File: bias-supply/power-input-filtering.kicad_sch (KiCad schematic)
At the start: 13 parts

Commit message: Updates for new bubba board
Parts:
- removed FL1, FL2: Choke_Coilcraft_MSD1278, MSD1278:MSD1278, symbol MSD1278:MSD1278
- added +V1: +V, bias-supply:TestPoint_THTPad_D2.0mm_Drill1.0mm_JLCrules, symbol Connector:TestPoint
- added -V1: -V, bias-supply:TestPoint_THTPad_D2.0mm_Drill1.0mm_JLCrules, symbol Connector:TestPoint
- added COM1: COM, bias-supply:TestPoint_THTPad_D2.0mm_Drill1.0mm_JLCrules, symbol Connector:TestPoint
- added FL1, FL2: Choke_Coilcraft_MSD1278, bias-supply:MSD1278, symbol bias-supply:MSD1278
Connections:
- net +V: now also +V1.1, FL1.4
- net -V: now also -V1.1, FL2.3
- net GND: no longer L1.2
- net COM IN: now reaches JP1.2 (B)
- net COM IN: now also C1.2, C2.2, C3.2, C4.2, JP2.1 (A), L1.1
- net +Vin renamed +VIN
- net +VIN: now also FL1.2
- net -Vin renamed -VIN
- net -VIN: now also FL2.1
- removed net REF: C1.2, C2.2, C3.2, C4.2, JP1.1 (A), JP2.2 (B), L1.1
- new net: FL1.1, JP1.1 (A)
- new net: FL2.2, JP2.2 (B)
- new net COM OUT: COM1.1, FL1.3, FL2.4, L1.2
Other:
- title: (none) -> Power input filtering
- moved on the sheet: C1, C2, C3, C4, C5, C6, C7, C8, L1

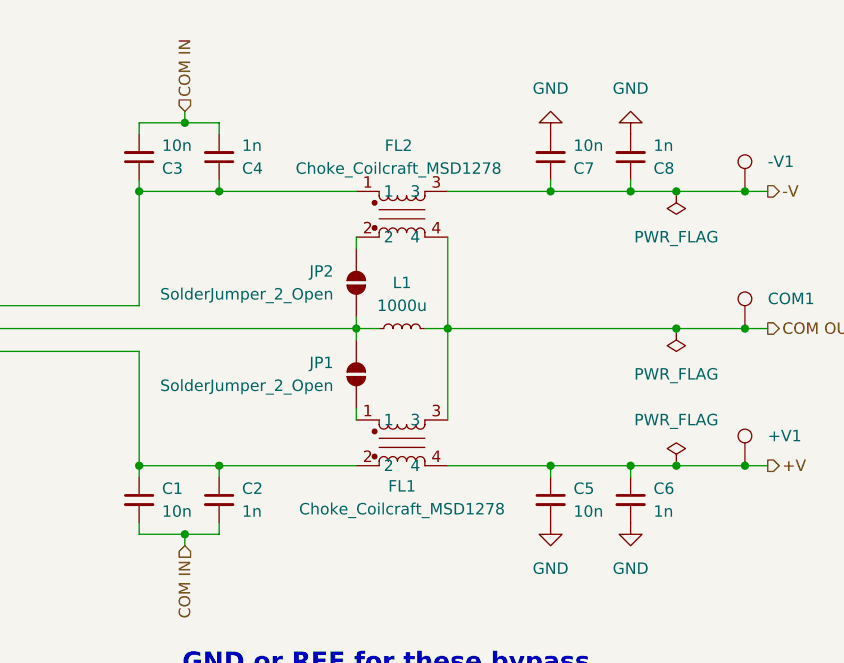
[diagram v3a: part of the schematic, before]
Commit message: Add fuses; change to coax; fixed I2C gnd
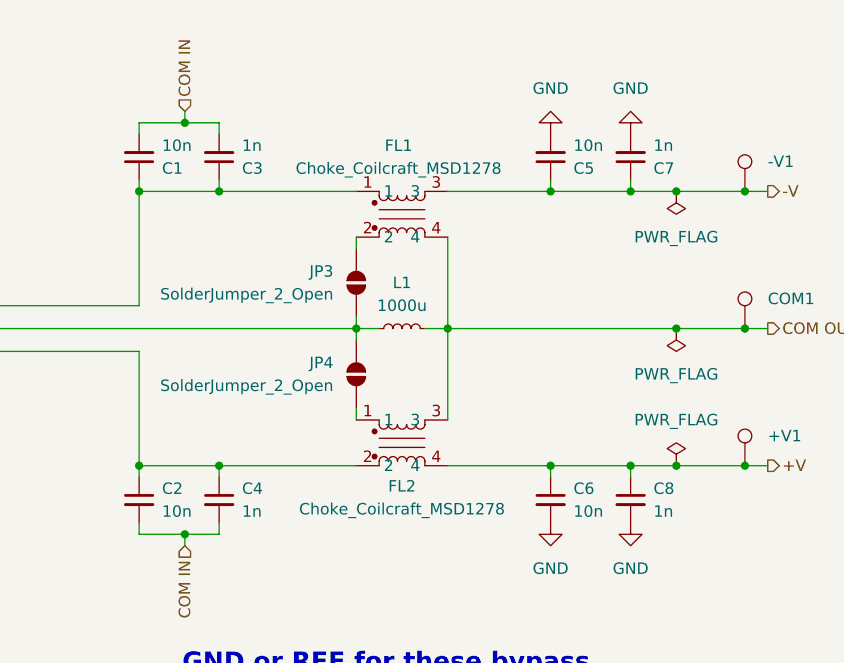
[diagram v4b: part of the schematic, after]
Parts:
- renumbered C3 to C1, C1 to C2, C4 to C3, C2 to C4, C7 to C5, C5 to C6, C8 to C7, C6 to C8, FL2 to FL1, FL1 to FL2, JP2 to JP3, JP1 to JP4
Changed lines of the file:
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@@
 		(dnp no)
 		(fields_autoplaced yes)
-		(property "Reference" "#PWR036"
+		(property "Reference" "#PWR05"
 			(at 166.37 114.3 0)
 			(effects
@@
 			(project "bias-supply"
 				(path "/f3205b63-fc57-4ea3-95d4-2a447f249c30/00549f8c-b970-4cd6-9099-4f1937ad6dc3"
-					(reference "#PWR036")
+					(reference "#PWR05")
 					(unit 1)
 				)
@@
 		(dnp no)
 		(fields_autoplaced yes)
-		(property "Reference" "#PWR034"
+		(property "Reference" "#PWR04"
 			(at 166.37 58.42 0)
 			(effects
@@
 			(project "bias-supply"
 				(path "/f3205b63-fc57-4ea3-95d4-2a447f249c30/00549f8c-b970-4cd6-9099-4f1937ad6dc3"
-					(reference "#PWR034")
+					(reference "#PWR04")
 					(unit 1)
 				)
@@
 		(on_board yes)
 		(dnp no)
-		(property "Reference" "FL1"
+		(property "Reference" "FL2"
 			(at 149.86 103.886 0)
 			(effects
@@
 			(project ""
 				(path "/f3205b63-fc57-4ea3-95d4-2a447f249c30/00549f8c-b970-4cd6-9099-4f1937ad6dc3"
-					(reference "FL1")
+					(reference "FL2")
 					(unit 1)
 				)
@@
 		(on_board yes)
 		(dnp no)
-		(property "Reference" "C8"
+		(property "Reference" "C7"
 			(at 177.8 68.5737 0)
 			(effects
@@
 			(project "bias-supply"
 				(path "/f3205b63-fc57-4ea3-95d4-2a447f249c30/00549f8c-b970-4cd6-9099-4f1937ad6dc3"
-					(reference "C8")
+					(reference "C7")
 					(unit 1)
 				)
@@
 		(dnp no)
 		(fields_autoplaced yes)
-		(property "Reference" "#FLG01"
+		(property "Reference" "#FLG04"
 			(at 180.34 88.265 0)
 			(effects
@@
 			(project "bias-supply"
 				(path "/f3205b63-fc57-4ea3-95d4-2a447f249c30/00549f8c-b970-4cd6-9099-4f1937ad6dc3"
-					(reference "#FLG01")
+					(reference "#FLG04")
 					(unit 1)
 				)
@@
 		(dnp no)
 		(fields_autoplaced yes)
-		(property "Reference" "#PWR042"
+		(property "Reference" "#PWR07"
 			(at 175.26 114.3 0)
 			(effects
@@
 			(project "bias-supply"
 				(path "/f3205b63-fc57-4ea3-95d4-2a447f249c30/00549f8c-b970-4cd6-9099-4f1937ad6dc3"
-					(reference "#PWR042")
+					(reference "#PWR07")
 					(unit 1)
 				)
@@
 		(on_board yes)
 		(dnp no)
-		(property "Reference" "C7"
+		(property "Reference" "C5"
 			(at 168.91 68.5737 0)
 			(effects
@@
 			(project "bias-supply"
 				(path "/f3205b63-fc57-4ea3-95d4-2a447f249c30/00549f8c-b970-4cd6-9099-4f1937ad6dc3"
-					(reference "C7")
+					(reference "C5")
 					(unit 1)
 				)
@@
 		(on_board yes)
 		(dnp no)
-		(property "Reference" "C5"
+		(property "Reference" "C6"
 			(at 168.91 104.1463 0)
 			(effects
@@
 			(project "bias-supply"
 				(path "/f3205b63-fc57-4ea3-95d4-2a447f249c30/00549f8c-b970-4cd6-9099-4f1937ad6dc3"
-					(reference "C5")
+					(reference "C6")
 					(unit 1)
 				)
@@
 		(on_board yes)
 		(dnp no)
-		(property "Reference" "C1"
+		(property "Reference" "C2"
 			(at 123.19 104.1463 0)
 			(effects
@@
 			(project "bias-supply"
 				(path "/f3205b63-fc57-4ea3-95d4-2a447f249c30/00549f8c-b970-4cd6-9099-4f1937ad6dc3"
-					(reference "C1")
+					(reference "C2")
 					(unit 1)
 				)
@@
 		(dnp no)
 		(fields_autoplaced yes)
-		(property "Reference" "#FLG03"
+		(property "Reference" "#FLG05"
 			(at 180.34 99.695 0)
 			(effects
@@
 			(project "bias-supply"
 				(path "/f3205b63-fc57-4ea3-95d4-2a447f249c30/00549f8c-b970-4cd6-9099-4f1937ad6dc3"
-					(reference "#FLG03")
+					(reference "#FLG05")
 					(unit 1)
 				)
@@
 		(dnp no)
 		(fields_autoplaced yes)
-		(property "Reference" "FL2"
+		(property "Reference" "FL1"
 			(at 149.479 66.04 0)
 			(effects
@@
 			(project ""
 				(path "/f3205b63-fc57-4ea3-95d4-2a447f249c30/00549f8c-b970-4cd6-9099-4f1937ad6dc3"
-					(reference "FL2")
+					(reference "FL1")
 					(unit 1)
 				)
@@
 		(on_board yes)
 		(dnp no)
-		(property "Reference" "C4"
+		(property "Reference" "C3"
 			(at 132.08 68.5737 0)
 			(effects
@@
 			(project "bias-supply"
 				(path "/f3205b63-fc57-4ea3-95d4-2a447f249c30/00549f8c-b970-4cd6-9099-4f1937ad6dc3"
-					(reference "C4")
+					(reference "C3")
 					(unit 1)
 				)
@@
 		(on_board yes)
 		(dnp no)
-		(property "Reference" "C2"
+		(property "Reference" "C4"
 			(at 132.08 104.1463 0)
 			(effects
@@
 			(project "bias-supply"
 				(path "/f3205b63-fc57-4ea3-95d4-2a447f249c30/00549f8c-b970-4cd6-9099-4f1937ad6dc3"
-					(reference "C2")
+					(reference "C4")
 					(unit 1)
 				)
@@
 		(dnp no)
 		(fields_autoplaced yes)
-		(property "Reference" "#FLG02"
+		(property "Reference" "#FLG03"
 			(at 180.34 73.025 0)
 			(effects
@@
 			(project "bias-supply"
 				(path "/f3205b63-fc57-4ea3-95d4-2a447f249c30/00549f8c-b970-4cd6-9099-4f1937ad6dc3"
-					(reference "#FLG02")
+					(reference "#FLG03")
 					(unit 1)
 				)
@@
 		(on_board yes)
 		(dnp no)
-		(property "Reference" "C6"
+		(property "Reference" "C8"
 			(at 177.8 104.1463 0)
 			(effects
@@
 			(project "bias-supply"
 				(path "/f3205b63-fc57-4ea3-95d4-2a447f249c30/00549f8c-b970-4cd6-9099-4f1937ad6dc3"
-					(reference "C6")
+					(reference "C8")
 					(unit 1)
 				)
@@
 		(on_board yes)
 		(dnp no)
-		(property "Reference" "JP1"
+		(property "Reference" "JP4"
 			(at 142.24 90.1699 90)
 			(effects
@@
 			(project ""
 				(path "/f3205b63-fc57-4ea3-95d4-2a447f249c30/00549f8c-b970-4cd6-9099-4f1937ad6dc3"
-					(reference "JP1")
+					(reference "JP4")
 					(unit 1)
 				)
@@
 		(dnp no)
 		(fields_autoplaced yes)
-		(property "Reference" "#PWR041"
+		(property "Reference" "#PWR06"
 			(at 175.26 58.42 0)
 			(effects
@@
 			(project "bias-supply"
 				(path "/f3205b63-fc57-4ea3-95d4-2a447f249c30/00549f8c-b970-4cd6-9099-4f1937ad6dc3"
-					(reference "#PWR041")
+					(reference "#PWR06")
 					(unit 1)
 				)
@@
 		(on_board yes)
 		(dnp no)
-		(property "Reference" "C3"
+		(property "Reference" "C1"
 			(at 123.19 68.5737 0)
 			(effects
@@
 			(project "bias-supply"
 				(path "/f3205b63-fc57-4ea3-95d4-2a447f249c30/00549f8c-b970-4cd6-9099-4f1937ad6dc3"
-					(reference "C3")
+					(reference "C1")
 					(unit 1)
 				)
@@
 		(on_board yes)
 		(dnp no)
-		(property "Reference" "JP2"
+		(property "Reference" "JP3"
 			(at 142.24 80.0099 90)
 			(effects
@@
 			(project "bias-supply"
 				(path "/f3205b63-fc57-4ea3-95d4-2a447f249c30/00549f8c-b970-4cd6-9099-4f1937ad6dc3"
-					(reference "JP2")
-					(unit 1)
-				)
+					(reference "JP3")
+					(unit 1)
+				)

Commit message: Bubba V2.1
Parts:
- +V1, -V1, COM1: now left out of the parts list
- L1: now not fitted; now left out of the parts list
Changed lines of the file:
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@@
 	(title_block
 		(title "Power input filtering")
-		(date "2025-06-12")
-		(rev "2.0")
+		(date "2026-03-05")
+		(rev "2.1")
 	)
 	(text "GND or REF for these bypass\ncapacitors on the input of the CMC???"
@@
 		(unit 1)
 		(exclude_from_sim no)
-		(in_bom yes)
+		(in_bom no)
 		(on_board yes)
-		(dnp no)
+		(dnp yes)
 		(property "Reference" "L1"
 			(at 149.86 81.28 90)
@@
 			)
 		)
-		(property "Datasheet" "~"
+		(property "Datasheet" "https://mm.digikey.com/Volume0/opasdata/d220001/medias/docus/4899/LSQx_Series_Cat.pdf"
 			(at 149.86 86.36 0)
 			(effects
@@
 			)
 		)
-		(property "Description" ""
+		(property "Description" "LSQBA321818T102K"
 			(at 149.86 86.36 0)
 			(effects
@@
 			)
 		)
-		(property "Datasheet" ""
+		(property "Datasheet" "https://www.coilcraft.com/getmedia/9bb1bfe8-4110-44c7-9e7e-54ca2b271b64/msd1278.pdf"
 			(at 149.86 99.06 0)
 			(effects
@@
 			)
 		)
-		(property "Description" ""
+		(property "Description" "MSD1278"
 			(at 149.86 99.06 0)
 			(effects
@@
 			)
 		)
-		(property "Datasheet" "~"
+		(property "Datasheet" "https://yageogroup.com/content/datasheet/asset/file/KEM_C1003_C0G_SMD"
 			(at 175.26 67.31 0)
 			(effects
@@
 			)
 		)
-		(property "Description" ""
+		(property "Description" "C1206C102J2GACTU"
 			(at 175.26 67.31 0)
 			(effects
@@
 			)
 		)
-		(property "Datasheet" "~"
+		(property "Datasheet" "https://search.murata.co.jp/Ceramy/image/img/A01X/G101/ENG/GCM3195C2A103GA16-01A.pdf"
 			(at 166.37 67.31 0)
 			(effects
@@
 			)
 		)
-		(property "Description" ""
+		(property "Description" "GCM3195C2A103GA16D"
 			(at 166.37 67.31 0)
 			(effects
@@
 			)
 		)
-		(property "Datasheet" "~"
+		(property "Datasheet" "https://search.murata.co.jp/Ceramy/image/img/A01X/G101/ENG/GCM3195C2A103GA16-01A.pdf"
 			(at 166.37 105.41 0)
 			(effects
@@
 			)
 		)
-		(property "Description" ""
+		(property "Description" "GCM3195C2A103GA16D"
 			(at 166.37 105.41 0)
 			(effects
@@
 			)
 		)
-		(property "Datasheet" "~"
+		(property "Datasheet" "https://search.murata.co.jp/Ceramy/image/img/A01X/G101/ENG/GCM3195C2A103GA16-01A.pdf"
 			(at 120.65 105.41 0)
 			(effects
@@
 			)
 		)
-		(property "Description" ""
+		(property "Description" "GCM3195C2A103GA16D"
 			(at 120.65 105.41 0)
 			(effects
@@
 			)
 		)
-		(property "Datasheet" ""
+		(property "Datasheet" "https://www.coilcraft.com/getmedia/9bb1bfe8-4110-44c7-9e7e-54ca2b271b64/msd1278.pdf"
 			(at 149.86 73.66 0)
 			(effects
@@
 			)
 		)
-		(property "Description" ""
+		(property "Description" "MSD1278-683MLD"
 			(at 149.86 73.66 0)
 			(effects
@@
 			)
 		)
-		(property "Datasheet" "~"
+		(property "Datasheet" "https://yageogroup.com/content/datasheet/asset/file/KEM_C1003_C0G_SMD"
 			(at 129.54 67.31 0)
 			(effects
@@
 			)
 		)
-		(property "Description" ""
+		(property "Description" "C1206C102J2GACTU"
 			(at 129.54 67.31 0)
 			(effects
@@
 		(unit 1)
 		(exclude_from_sim no)
-		(in_bom yes)
+		(in_bom no)
 		(on_board yes)
 		(dnp no)
@@
 			)
 		)
-		(property "Datasheet" "~"
+		(property "Datasheet" "https://yageogroup.com/content/datasheet/asset/file/KEM_C1003_C0G_SMD"
 			(at 129.54 105.41 0)
 			(effects
@@
 			)
 		)
-		(property "Description" ""
+		(property "Description" "C1206C102J2GACTU"
 			(at 129.54 105.41 0)
 			(effects
@@
 			)
 		)
-		(property "Datasheet" "~"
+		(property "Datasheet" "https://yageogroup.com/content/datasheet/asset/file/KEM_C1003_C0G_SMD"
 			(at 175.26 105.41 0)
 			(effects
@@
 			)
 		)
-		(property "Description" ""
+		(property "Description" "C1206C102J2GACTU"
 			(at 175.26 105.41 0)
 			(effects
@@
 			)
 		)
-		(property "Datasheet" "~"
+		(property "Datasheet" "https://search.murata.co.jp/Ceramy/image/img/A01X/G101/ENG/GCM3195C2A103GA16-01A.pdf"
 			(at 120.65 67.31 0)
 			(effects
@@
 			)
 		)
-		(property "Description" ""
+		(property "Description" "GCM3195C2A103GA16D"
 			(at 120.65 67.31 0)
 			(effects
@@
 		(unit 1)
 		(exclude_from_sim no)
-		(in_bom yes)
+		(in_bom no)
 		(on_board yes)
 		(dnp no)
@@
 		(unit 1)
 		(exclude_from_sim no)
-		(in_bom yes)
+		(in_bom no)
 		(on_board yes)
 		(dnp no)
